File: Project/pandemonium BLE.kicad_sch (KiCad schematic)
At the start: 112 parts, among them J1 HRO_TYPE-C-31-M-14, J3 Battery, J7 TC2030_SWD, Q1 AO3407, SW1 RotaryEncoder_Switch, SW2 RotaryEncoder_Switch, U2 HOLYIOT-18010, U3 MCP73831, U4 USBLC6-2P6, U8 XC6206PxxxMR

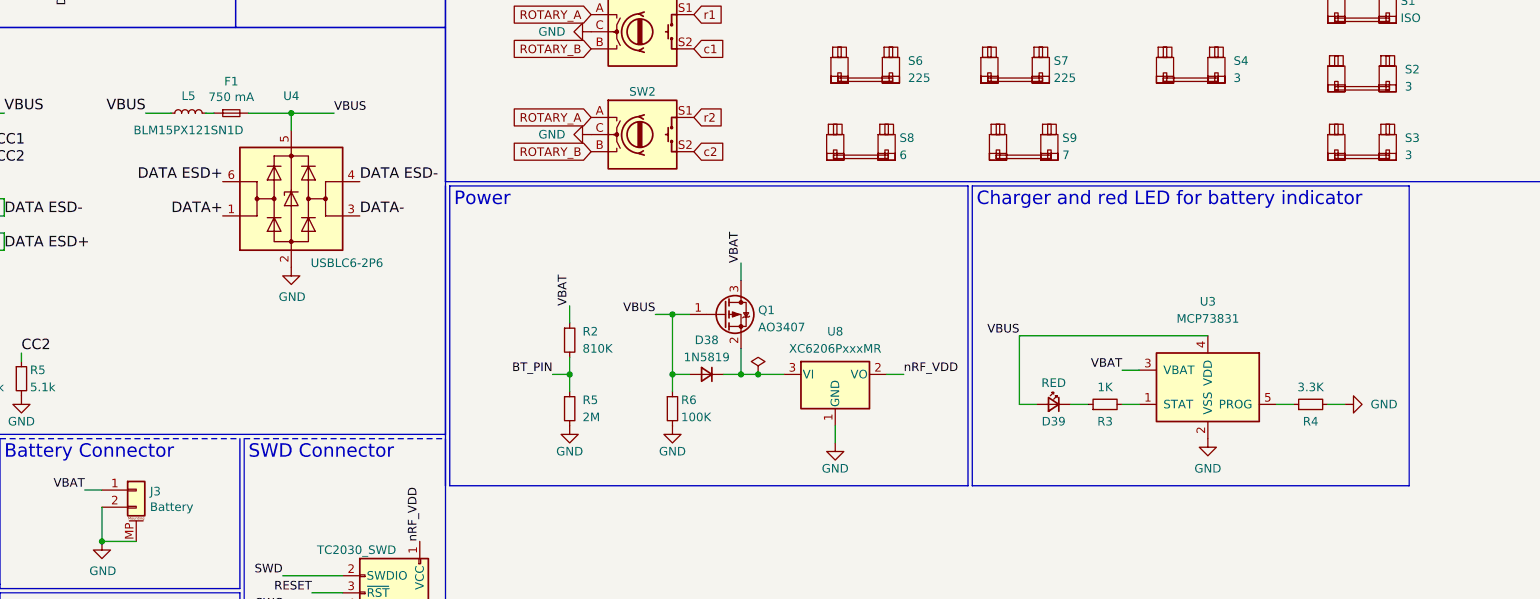
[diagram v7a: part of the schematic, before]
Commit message: changes to topre version and BLE version
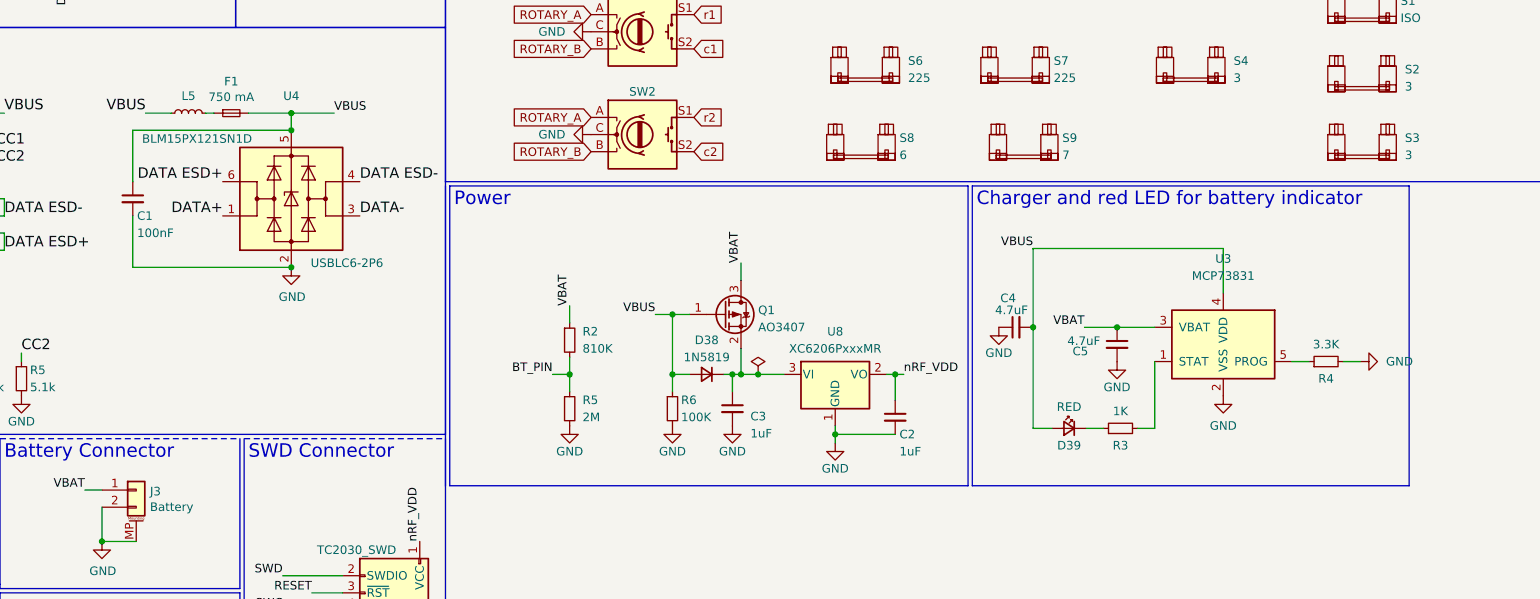
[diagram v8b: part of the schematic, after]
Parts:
- added C1: 100nF, Capacitor_SMD:C_0402_1005Metric, symbol Device:C_Small
- added C2, C3: 1uF, Capacitor_SMD:C_0402_1005Metric, symbol Device:C_Small
- added C4, C5: 4.7uF, Capacitor_SMD:C_0402_1005Metric, symbol Device:C_Small
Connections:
- net GND: now also C1.2, C2.2, C3.2, C4.1, C5.2
- net VBAT: now also C5.1
- net VBUS: now also C1.1, C4.2
- net nRF_VDD: now also C2.1
- net at D38.1 (K), Q1.2 (S), U8.3 (VI): now also C3.1
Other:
- moved on the sheet: D39, R3, R4, U3
